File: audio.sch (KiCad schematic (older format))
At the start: 37 parts

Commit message: switch Z_out resistors to 2 ohms & select components
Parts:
- R? (x4): value 4 -> 2; footprint (none) -> Resistor_THT:R_Axial_DIN0411_L9.9mm_D3.6mm_P15.24mm_Horizontal; Description (none) -> Metal Film Resistors - Through Hole 2ohms 1% 100PPM; Manufacturer (none) -> KOA Speer; Manufacturer Part Number (none) -> MF1/2DCT52R2R00F; Supplier (none) -> Mouser; Supplier Part Number (none) -> 660-MF1/2DCT52R2R00F
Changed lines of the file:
@@
 AR Path="/5CB56C16/5CE9DF83" Ref="R?"  Part="1"
 F 0 "R?" V 8780 2950 50  0000 C CNN
-F 1 "4" V 8700 2950 50  0000 C CNN
-F 2 "" V 8630 2950 50  0001 C CNN
-F 3 "" H 8700 2950 50  0001 C CNN
-F 4 "" H 8700 2950 50  0001 C CNN "Description"
-F 5 "" H 8700 2950 50  0001 C CNN "Manufacturer"
-F 6 "" H 8700 2950 50  0001 C CNN "Manufacturer Part Number"
-F 7 "" H 8700 2950 50  0001 C CNN "Supplier"
-F 8 "" H 8700 2950 50  0001 C CNN "Supplier Part Number"
+F 1 "2" V 8700 2950 50  0000 C CNN
+F 2 "Resistor_THT:R_Axial_DIN0411_L9.9mm_D3.6mm_P15.24mm_Horizontal" V 8630 2950 50  0001 C CNN
+F 3 "https://www.mouser.com/datasheet/2/219/MF-MFS-RK-18760.pdf" H 8700 2950 50  0001 C CNN
+F 4 "Metal Film Resistors - Through Hole 2ohms 1% 100PPM" H 8700 2950 50  0001 C CNN "Description"
+F 5 "KOA Speer" H 8700 2950 50  0001 C CNN "Manufacturer"
+F 6 "MF1/2DCT52R2R00F" H 8700 2950 50  0001 C CNN "Manufacturer Part Number"
+F 7 "Mouser" H 8700 2950 50  0001 C CNN "Supplier"
+F 8 "660-MF1/2DCT52R2R00F" H 8700 2950 50  0001 C CNN "Supplier Part Number"
 	1    8700 2950
 	0    -1   -1   0
@@
 AR Path="/5CB56C16/5CEA3FB8" Ref="R?"  Part="1"
 F 0 "R?" V 8780 3550 50  0000 C CNN
-F 1 "4" V 8700 3550 50  0000 C CNN
-F 2 "" V 8630 3550 50  0001 C CNN
-F 3 "" H 8700 3550 50  0001 C CNN
-F 4 "" H 8700 3550 50  0001 C CNN "Description"
-F 5 "" H 8700 3550 50  0001 C CNN "Manufacturer"
-F 6 "" H 8700 3550 50  0001 C CNN "Manufacturer Part Number"
-F 7 "" H 8700 3550 50  0001 C CNN "Supplier"
-F 8 "" H 8700 3550 50  0001 C CNN "Supplier Part Number"
+F 1 "2" V 8700 3550 50  0000 C CNN
+F 2 "Resistor_THT:R_Axial_DIN0411_L9.9mm_D3.6mm_P15.24mm_Horizontal" V 8630 3550 50  0001 C CNN
+F 3 "https://www.mouser.com/datasheet/2/219/MF-MFS-RK-18760.pdf" H 8700 3550 50  0001 C CNN
+F 4 "Metal Film Resistors - Through Hole 2ohms 1% 100PPM" H 8700 3550 50  0001 C CNN "Description"
+F 5 "KOA Speer" H 8700 3550 50  0001 C CNN "Manufacturer"
+F 6 "MF1/2DCT52R2R00F" H 8700 3550 50  0001 C CNN "Manufacturer Part Number"
+F 7 "Mouser" H 8700 3550 50  0001 C CNN "Supplier"
+F 8 "660-MF1/2DCT52R2R00F" H 8700 3550 50  0001 C CNN "Supplier Part Number"
 	1    8700 3550
 	0    -1   1    0
@@
 AR Path="/5CB56C16/5CEC958E" Ref="R?"  Part="1"
 F 0 "R?" V 8780 4450 50  0000 C CNN
-F 1 "4" V 8700 4450 50  0000 C CNN
-F 2 "" V 8630 4450 50  0001 C CNN
-F 3 "" H 8700 4450 50  0001 C CNN
-F 4 "" H 8700 4450 50  0001 C CNN "Description"
-F 5 "" H 8700 4450 50  0001 C CNN "Manufacturer"
-F 6 "" H 8700 4450 50  0001 C CNN "Manufacturer Part Number"
-F 7 "" H 8700 4450 50  0001 C CNN "Supplier"
-F 8 "" H 8700 4450 50  0001 C CNN "Supplier Part Number"
+F 1 "2" V 8700 4450 50  0000 C CNN
+F 2 "Resistor_THT:R_Axial_DIN0411_L9.9mm_D3.6mm_P15.24mm_Horizontal" V 8630 4450 50  0001 C CNN
+F 3 "https://www.mouser.com/datasheet/2/219/MF-MFS-RK-18760.pdf" H 8700 4450 50  0001 C CNN
+F 4 "Metal Film Resistors - Through Hole 2ohms 1% 100PPM" H 8700 4450 50  0001 C CNN "Description"
+F 5 "KOA Speer" H 8700 4450 50  0001 C CNN "Manufacturer"
+F 6 "MF1/2DCT52R2R00F" H 8700 4450 50  0001 C CNN "Manufacturer Part Number"
+F 7 "Mouser" H 8700 4450 50  0001 C CNN "Supplier"
+F 8 "660-MF1/2DCT52R2R00F" H 8700 4450 50  0001 C CNN "Supplier Part Number"
 	1    8700 4450
 	0    -1   -1   0
@@
 AR Path="/5CB56C16/5CEC959D" Ref="R?"  Part="1"
 F 0 "R?" V 8780 5050 50  0000 C CNN
-F 1 "4" V 8700 5050 50  0000 C CNN
-F 2 "" V 8630 5050 50  0001 C CNN
-F 3 "" H 8700 5050 50  0001 C CNN
-F 4 "" H 8700 5050 50  0001 C CNN "Description"
-F 5 "" H 8700 5050 50  0001 C CNN "Manufacturer"
-F 6 "" H 8700 5050 50  0001 C CNN "Manufacturer Part Number"
-F 7 "" H 8700 5050 50  0001 C CNN "Supplier"
-F 8 "" H 8700 5050 50  0001 C CNN "Supplier Part Number"
+F 1 "2" V 8700 5050 50  0000 C CNN
+F 2 "Resistor_THT:R_Axial_DIN0411_L9.9mm_D3.6mm_P15.24mm_Horizontal" V 8630 5050 50  0001 C CNN
+F 3 "https://www.mouser.com/datasheet/2/219/MF-MFS-RK-18760.pdf" H 8700 5050 50  0001 C CNN
+F 4 "Metal Film Resistors - Through Hole 2ohms 1% 100PPM" H 8700 5050 50  0001 C CNN "Description"
+F 5 "KOA Speer" H 8700 5050 50  0001 C CNN "Manufacturer"
+F 6 "MF1/2DCT52R2R00F" H 8700 5050 50  0001 C CNN "Manufacturer Part Number"
+F 7 "Mouser" H 8700 5050 50  0001 C CNN "Supplier"
+F 8 "660-MF1/2DCT52R2R00F" H 8700 5050 50  0001 C CNN "Supplier Part Number"
 	1    8700 5050
 	0    -1   1    0

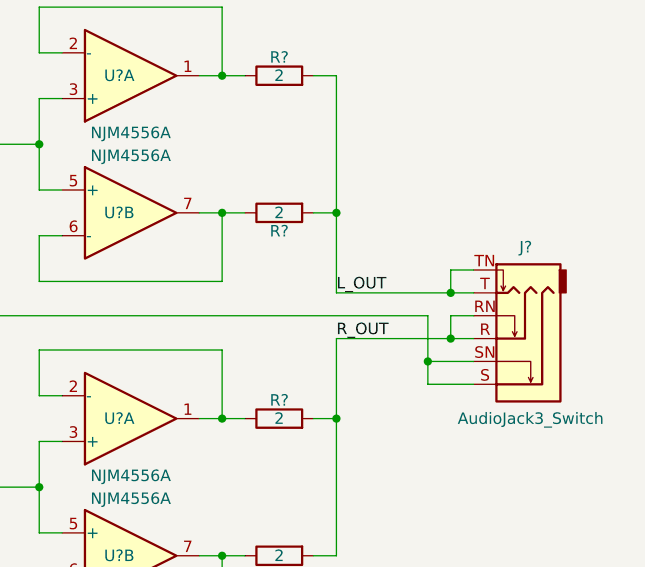
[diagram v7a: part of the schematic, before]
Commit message: add ic sockets for the 3 op amps
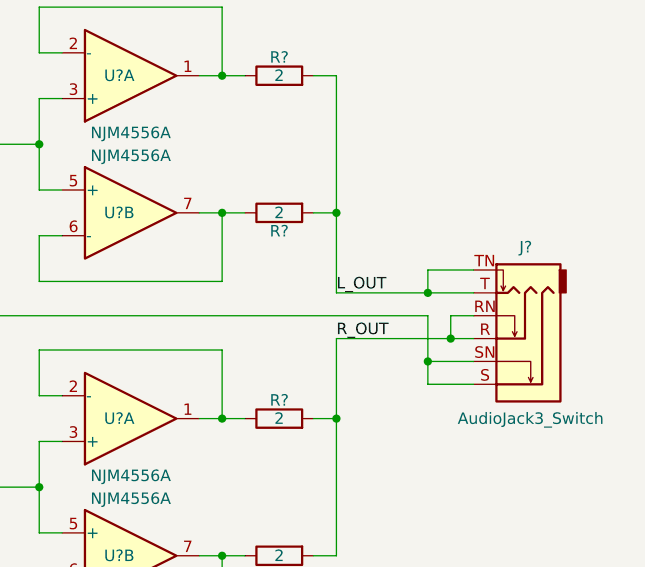
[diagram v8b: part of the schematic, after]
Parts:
- U? (x3): footprint (none) -> Package_DIP:DIP-8_W7.62mm_Socket_LongPads; Description (none) -> CONN IC DIP SOCKET 8POS TIN; Manufacturer (none) -> TE Connectivity AMP Connectors; Manufacturer Part Number (none) -> 1-2199298-2; Supplier (none) -> Digi-Key; Supplier Part Number (none) -> A120347-ND
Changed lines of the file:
@@
 F 0 "U?" H 8000 2950 50  0000 C CNN
 F 1 "NJM4556A" H 8050 3200 50  0000 C CNN
-F 2 "" H 8050 2950 50  0001 C CNN
-F 3 "http://www.njr.com/semicon/PDF/NJM4556A_E.pdf" H 8050 2950 50  0001 C CNN
+F 2 "Package_DIP:DIP-8_W7.62mm_Socket_LongPads" H 8050 2950 50  0001 C CNN
+F 3 "https://www.te.com/commerce/DocumentDelivery/DDEController?Action=srchrtrv&DocNm=2199298&DocType=Customer+Drawing&DocLang=English" H 8050 2950 50  0001 C CNN
+F 4 "CONN IC DIP SOCKET 8POS TIN" H 0   0   50  0001 C CNN "Description"
+F 5 "TE Connectivity AMP Connectors" H 0   0   50  0001 C CNN "Manufacturer"
+F 6 "1-2199298-2" H 0   0   50  0001 C CNN "Manufacturer Part Number"
+F 7 "Digi-Key" H 0   0   50  0001 C CNN "Supplier"
+F 8 "A120347-ND" H 0   0   50  0001 C CNN "Supplier Part Number"
 	1    8050 2950
 	1    0    0    1
@@
 F 0 "U?" H 5550 3000 50  0000 C CNN
 F 1 "NJM2068" H 5600 3250 50  0000 C CNN
-F 2 "" H 5600 3000 50  0001 C CNN
-F 3 "" H 5600 3000 50  0001 C CNN
+F 2 "Package_DIP:DIP-8_W7.62mm_Socket_LongPads" H 5600 3000 50  0001 C CNN
+F 3 "https://www.te.com/commerce/DocumentDelivery/DDEController?Action=srchrtrv&DocNm=2199298&DocType=Customer+Drawing&DocLang=English" H 5600 3000 50  0001 C CNN
+F 4 "CONN IC DIP SOCKET 8POS TIN" H 0   0   50  0001 C CNN "Description"
+F 5 "TE Connectivity AMP Connectors" H 0   0   50  0001 C CNN "Manufacturer"
+F 6 "1-2199298-2" H 0   0   50  0001 C CNN "Manufacturer Part Number"
+F 7 "Digi-Key" H 0   0   50  0001 C CNN "Supplier"
+F 8 "A120347-ND" H 0   0   50  0001 C CNN "Supplier Part Number"
 	1    5600 3000
 	1    0    0    -1
@@
 F 2 "" H 5600 5000 50  0001 C CNN
 F 3 "" H 5600 5000 50  0001 C CNN
+F 4 "" H 0   0   50  0001 C CNN "Description"
+F 5 "" H 0   0   50  0001 C CNN "Manufacturer"
+F 6 "" H 0   0   50  0001 C CNN "Manufacturer Part Number"
+F 7 "" H 0   0   50  0001 C CNN "Supplier"
+F 8 "" H 0   0   50  0001 C CNN "Supplier Part Number"
 	2    5600 5000
 	1    0    0    1
@@
 F 2 "" H 1700 1300 50  0001 C CNN
 F 3 "" H 1700 1300 50  0001 C CNN
+F 4 "" H 0   0   50  0001 C CNN "Description"
+F 5 "" H 0   0   50  0001 C CNN "Manufacturer"
+F 6 "" H 0   0   50  0001 C CNN "Manufacturer Part Number"
+F 7 "" H 0   0   50  0001 C CNN "Supplier"
+F 8 "" H 0   0   50  0001 C CNN "Supplier Part Number"
 	3    1700 1300
 	1    0    0    -1
@@
 F 0 "U?" H 8000 4450 50  0000 C CNN
 F 1 "NJM4556A" H 8050 4700 50  0000 C CNN
-F 2 "" H 8050 4450 50  0001 C CNN
-F 3 "http://www.njr.com/semicon/PDF/NJM4556A_E.pdf" H 8050 4450 50  0001 C CNN
+F 2 "Package_DIP:DIP-8_W7.62mm_Socket_LongPads" H 8050 4450 50  0001 C CNN
+F 3 "https://www.te.com/commerce/DocumentDelivery/DDEController?Action=srchrtrv&DocNm=2199298&DocType=Customer+Drawing&DocLang=English" H 8050 4450 50  0001 C CNN
+F 4 "CONN IC DIP SOCKET 8POS TIN" H 0   0   50  0001 C CNN "Description"
+F 5 "TE Connectivity AMP Connectors" H 0   0   50  0001 C CNN "Manufacturer"
+F 6 "1-2199298-2" H 0   0   50  0001 C CNN "Manufacturer Part Number"
+F 7 "Digi-Key" H 0   0   50  0001 C CNN "Supplier"
+F 8 "A120347-ND" H 0   0   50  0001 C CNN "Supplier Part Number"
 	1    8050 4450
 	1    0    0    1
@@
 Connection ~ 8950 3550
 Wire Wire Line
-	9550 3800 9450 3800
+	9550 3800 9350 3800
 $Comp
 L Device:R_POT_Dual_Separate RV?
@@
 	9450 4100 9550 4100
 Wire Wire Line
-	8950 3900 9450 3900
-Wire Wire Line
-	9450 3800 9450 3900
-Connection ~ 9450 3900
-Wire Wire Line
-	9450 3900 9550 3900
+	8950 3900 9350 3900
+Wire Wire Line
+	9350 3800 9350 3900
+Connection ~ 9350 3900
+Wire Wire Line
+	9350 3900 9550 3900
 Wire Wire Line
 	7350 4000 9350 4000
